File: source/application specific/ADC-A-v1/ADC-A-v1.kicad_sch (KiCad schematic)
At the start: 55 parts, among them IC1 MCP1725-1802E_SN, U1 AD4630-24BBCZ, U2 TXB0108DQSR, U3 TXB0108DQSR

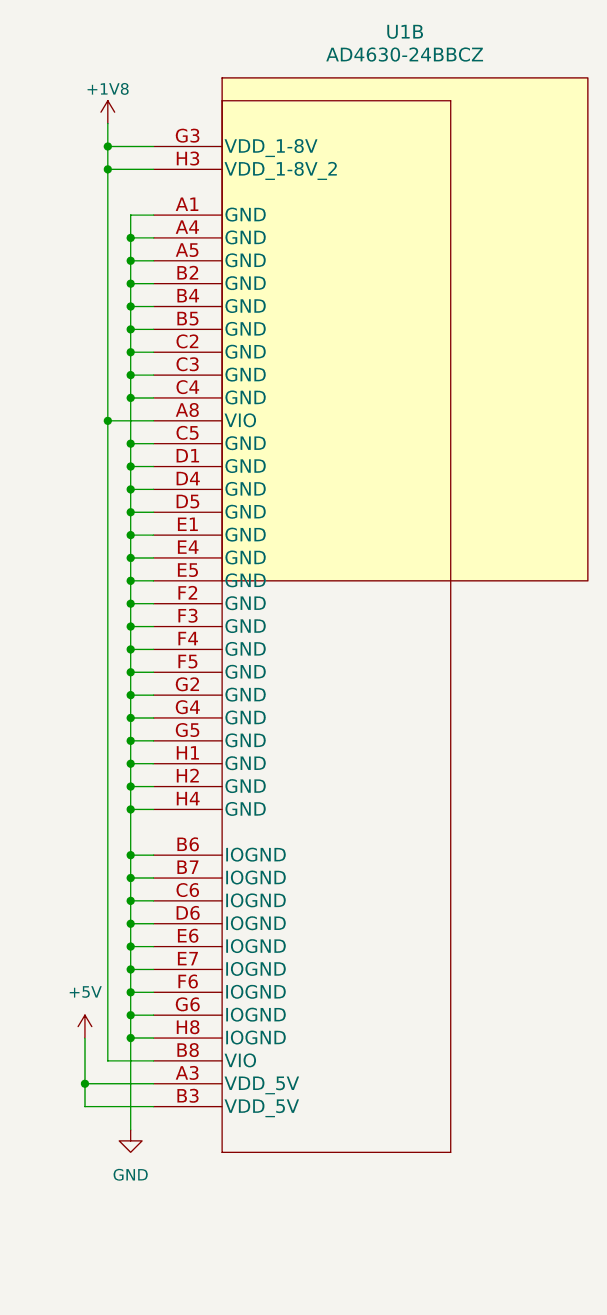
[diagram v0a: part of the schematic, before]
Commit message: Update ADC-A-v1.kicad_sch
Fixed AD4630 schematic symbol issue
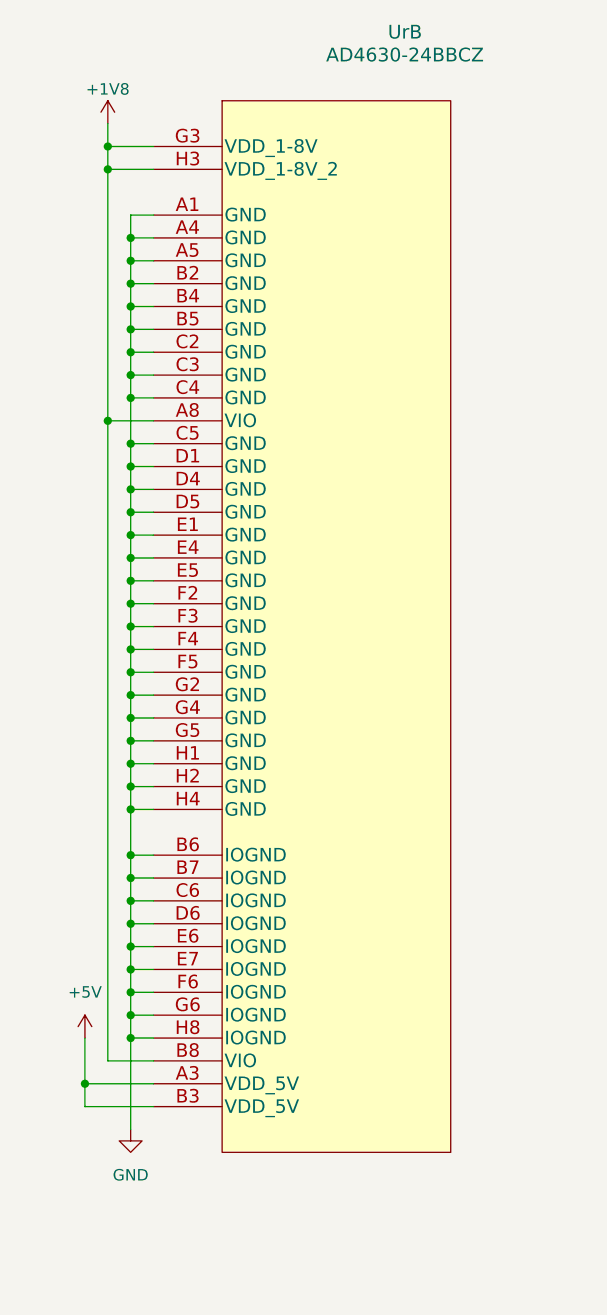
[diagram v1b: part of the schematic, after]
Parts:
- renumbered U1 to Ur
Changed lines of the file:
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@@
 		(dnp no)
 		(fields_autoplaced yes)
-		(property "Reference" "U1"
+		(property "Reference" "Ur"
 			(at 344.17 50.165 0)
 			(effects
@@
 			(project "ADC-A-v1"
 				(path "/575ab75a-f9eb-460a-bea6-cc97d23e4f1c"
-					(reference "U1")
+					(reference "Ur")
 					(unit 2)
 				)
